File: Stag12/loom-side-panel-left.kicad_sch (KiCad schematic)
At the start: 4 parts, among them SW10 SW_SPST

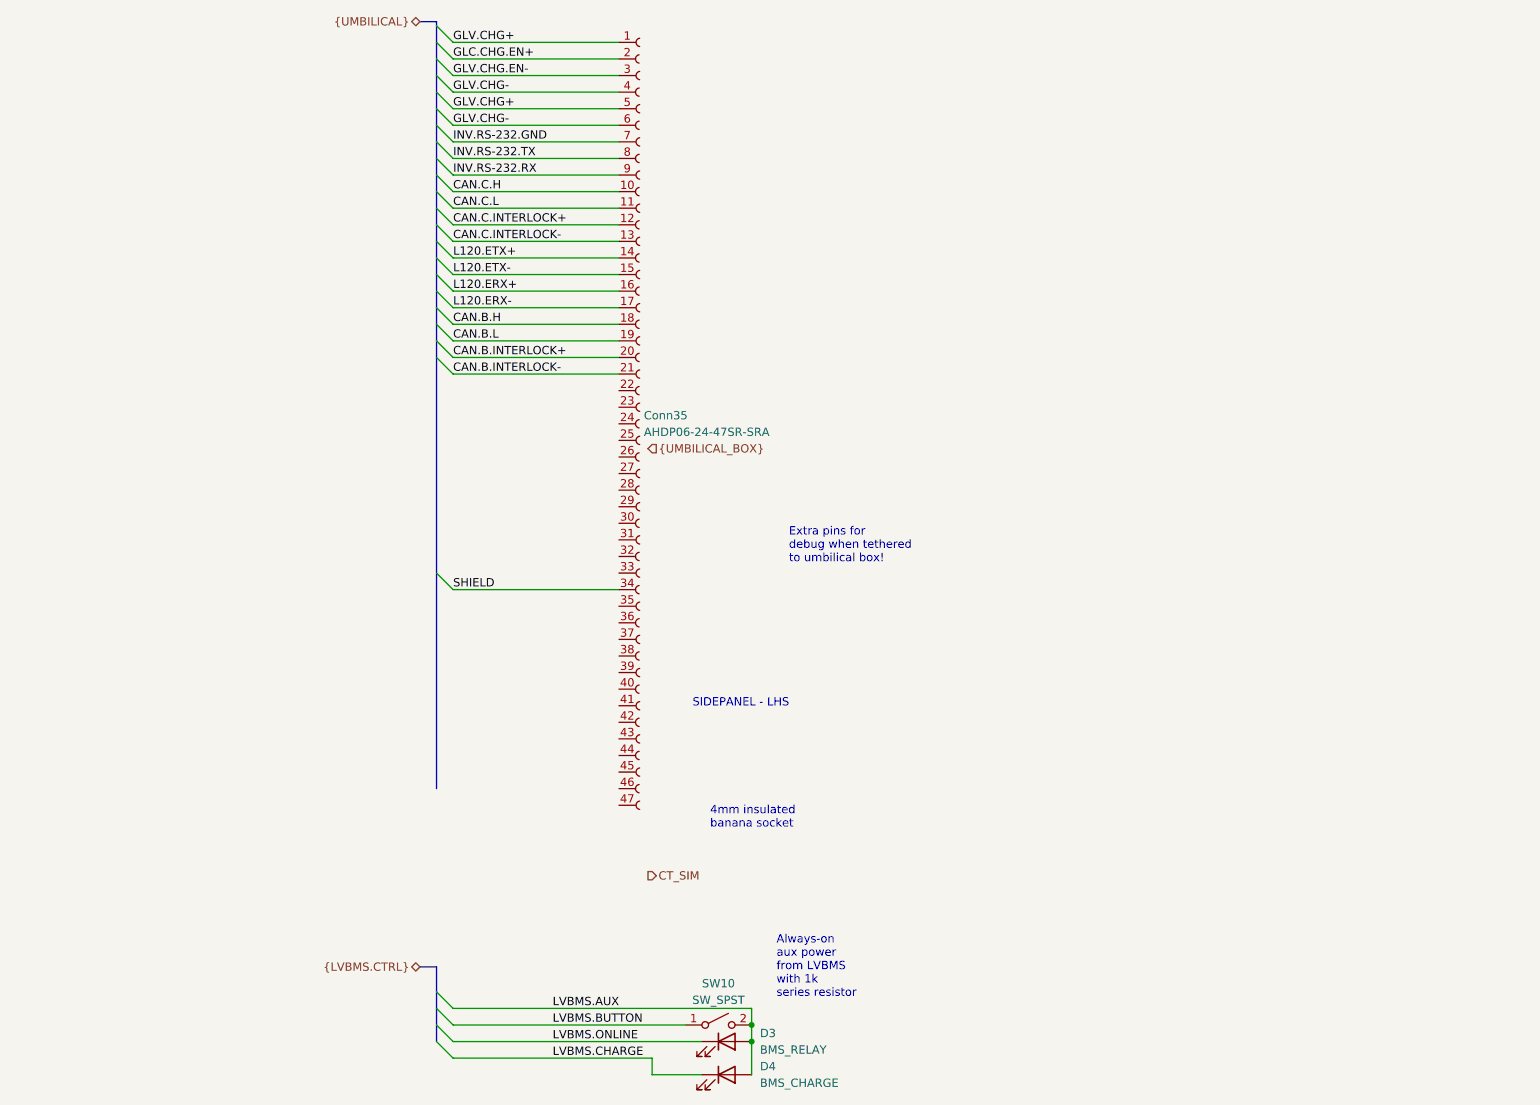
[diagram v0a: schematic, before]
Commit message: Started rear loom
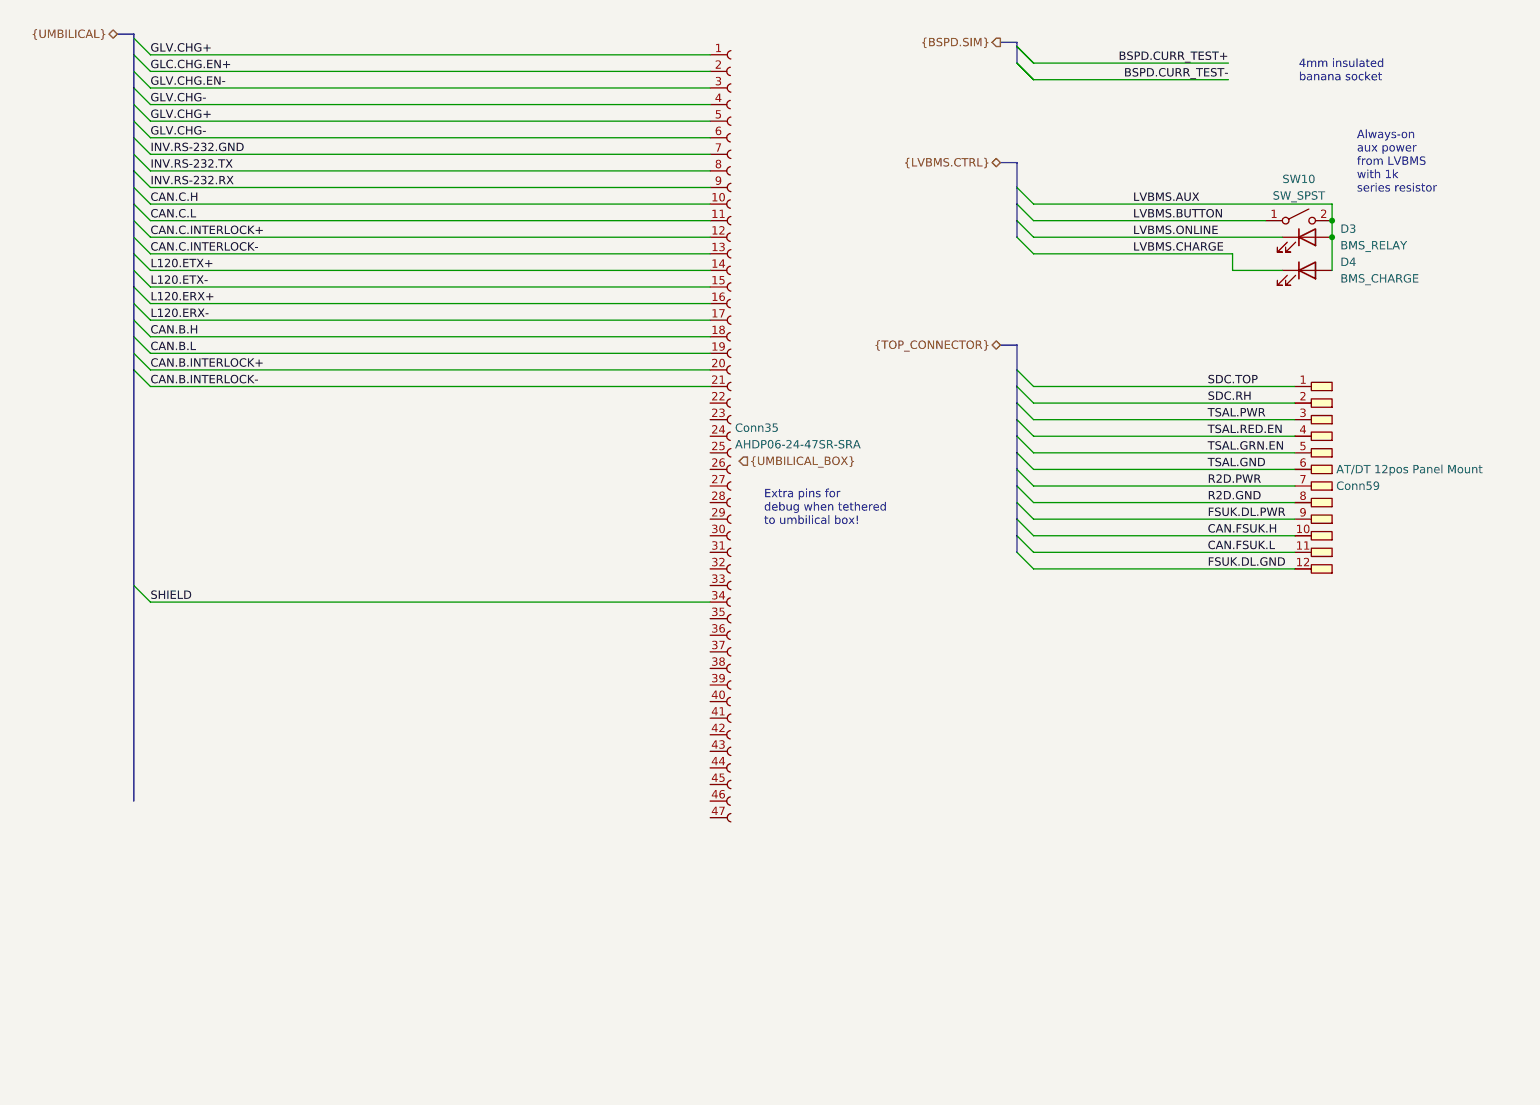
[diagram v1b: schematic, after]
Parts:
- added Conn59: AMPHENOL-21P-Pannel, symbol Connectors_SUFST:Deutsch_DTM_12P_Pin
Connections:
- new net CAN.FSUK.H: Conn59.10
- new net CAN.FSUK.L: Conn59.11
- new net FSUK.DL.GND: Conn59.12
- new net FSUK.DL.PWR: Conn59.9
- new net R2D.GND: Conn59.8
- new net R2D.PWR: Conn59.7
- new net SDC.RH: Conn59.2
- new net SDC.TOP: Conn59.1
- new net TSAL.GND: Conn59.6
- new net TSAL.GRN.EN: Conn59.5
- new net TSAL.PWR: Conn59.3
- new net TSAL.RED.EN: Conn59.4
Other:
- note removed: "SIDEPANEL - LHS"
- moved on the sheet: Conn35, D3, D4, SW10
